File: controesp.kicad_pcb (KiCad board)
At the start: 2 copper layers, 86.5 x 84 mm, 53 parts, among them J1 Screw_Terminal_01x02, J10 Screw_Terminal_01x04, J11 Screw_Terminal_01x04, J12 Screw_Terminal_01x04, J14 Conn_01x16_Socket, J15 Screw_Terminal_01x02, J2 Screw_Terminal_01x04, J3 Conn_01x14_Socket, J4 Conn_01x14_Pin, J5 Conn_01x16_Pin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

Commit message: small progress on pcb
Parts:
- moved J6 79.1 mm to (67.5, 53.4), turned to 180 degrees
- moved J5 78.4 mm to (218.2, 67.0), turned to 90 degrees
- moved J2 77.2 mm to (101.3, 53.5), turned to 180 degrees
- moved J8 74.3 mm to (118.0, 53.4), turned to 180 degrees
- moved J3 73.5 mm to (78.5, 106.0), turned to 90 degrees
- moved J14 73.2 mm to (73.9, 74.5), turned to 90 degrees
- moved K1 69.5 mm to (40.5, 173.6)
- moved K2 69.5 mm to (57.0, 173.5)
- moved K3 69.5 mm to (40.5, 153.0)
- moved K4 69.5 mm to (56.5, 153.0)
- moved K5 69.5 mm to (73.0, 173.5)
- moved K6 69.5 mm to (89.5, 173.3)
- moved K7 69.5 mm to (73.0, 153.0)
- moved K8 69.5 mm to (89.5, 153.0)
- moved J7 68.0 mm to (84.5, 53.4), turned to 180 degrees
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
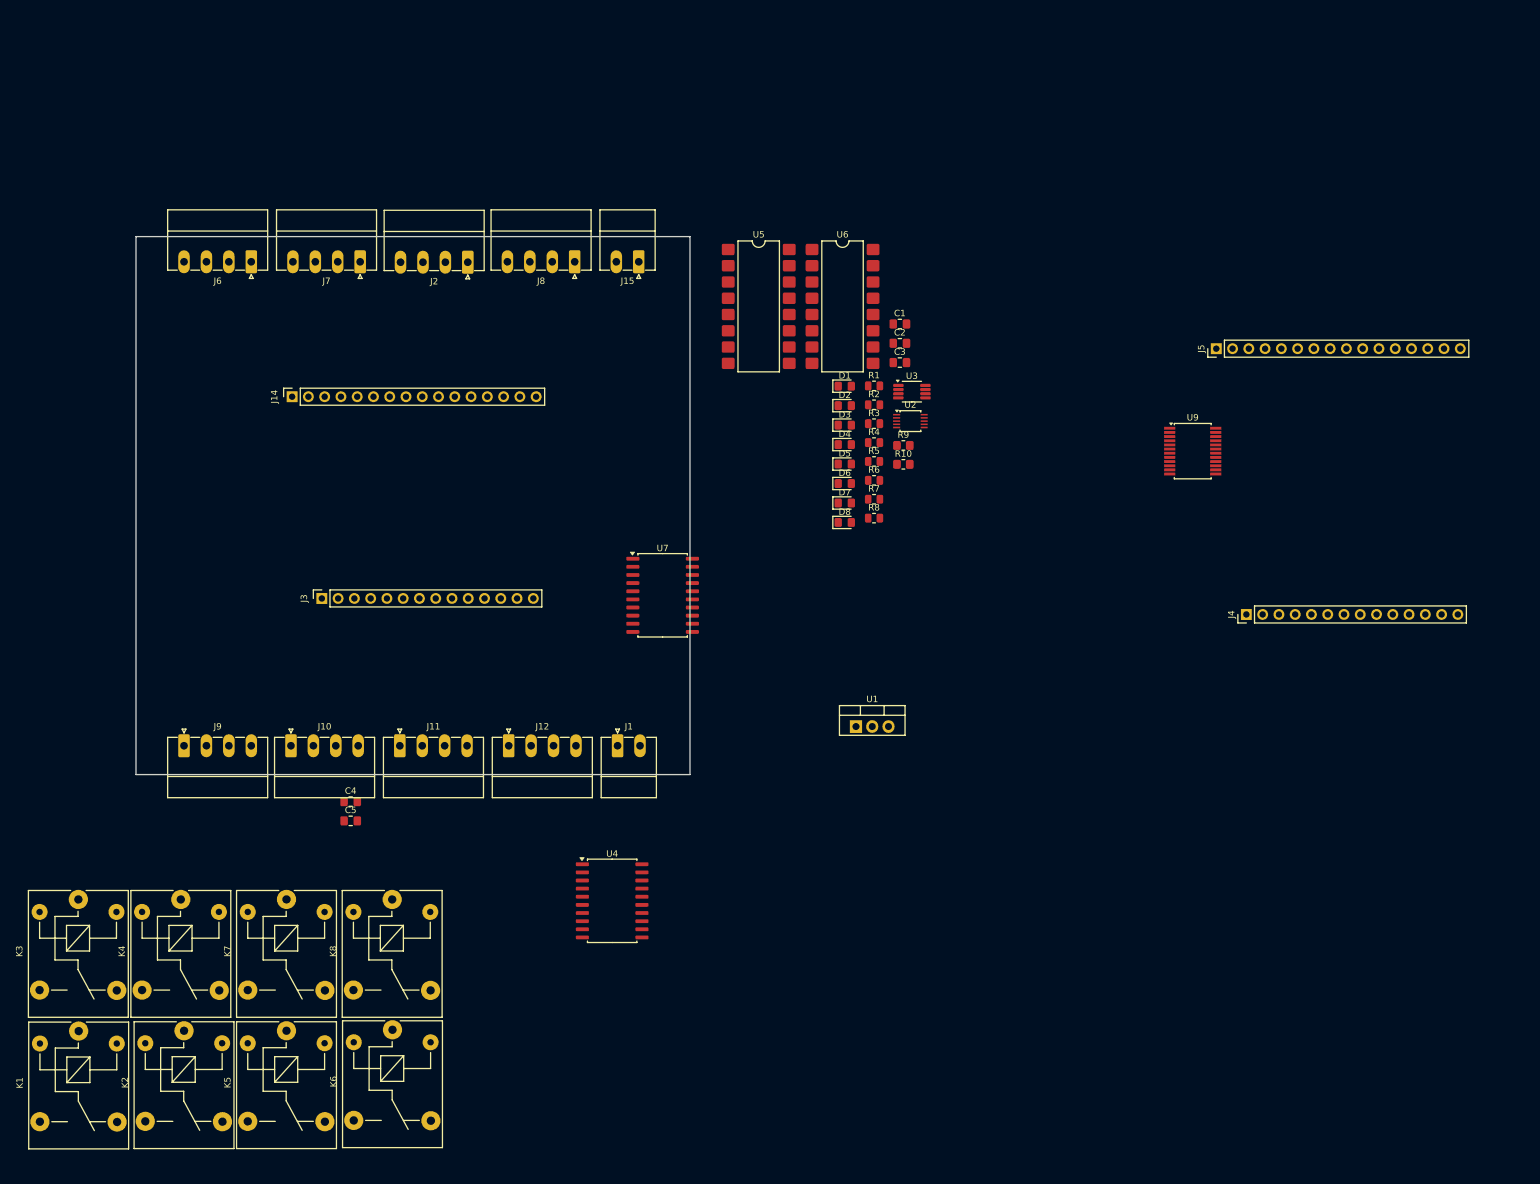
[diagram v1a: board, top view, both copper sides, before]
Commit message: larger pcb
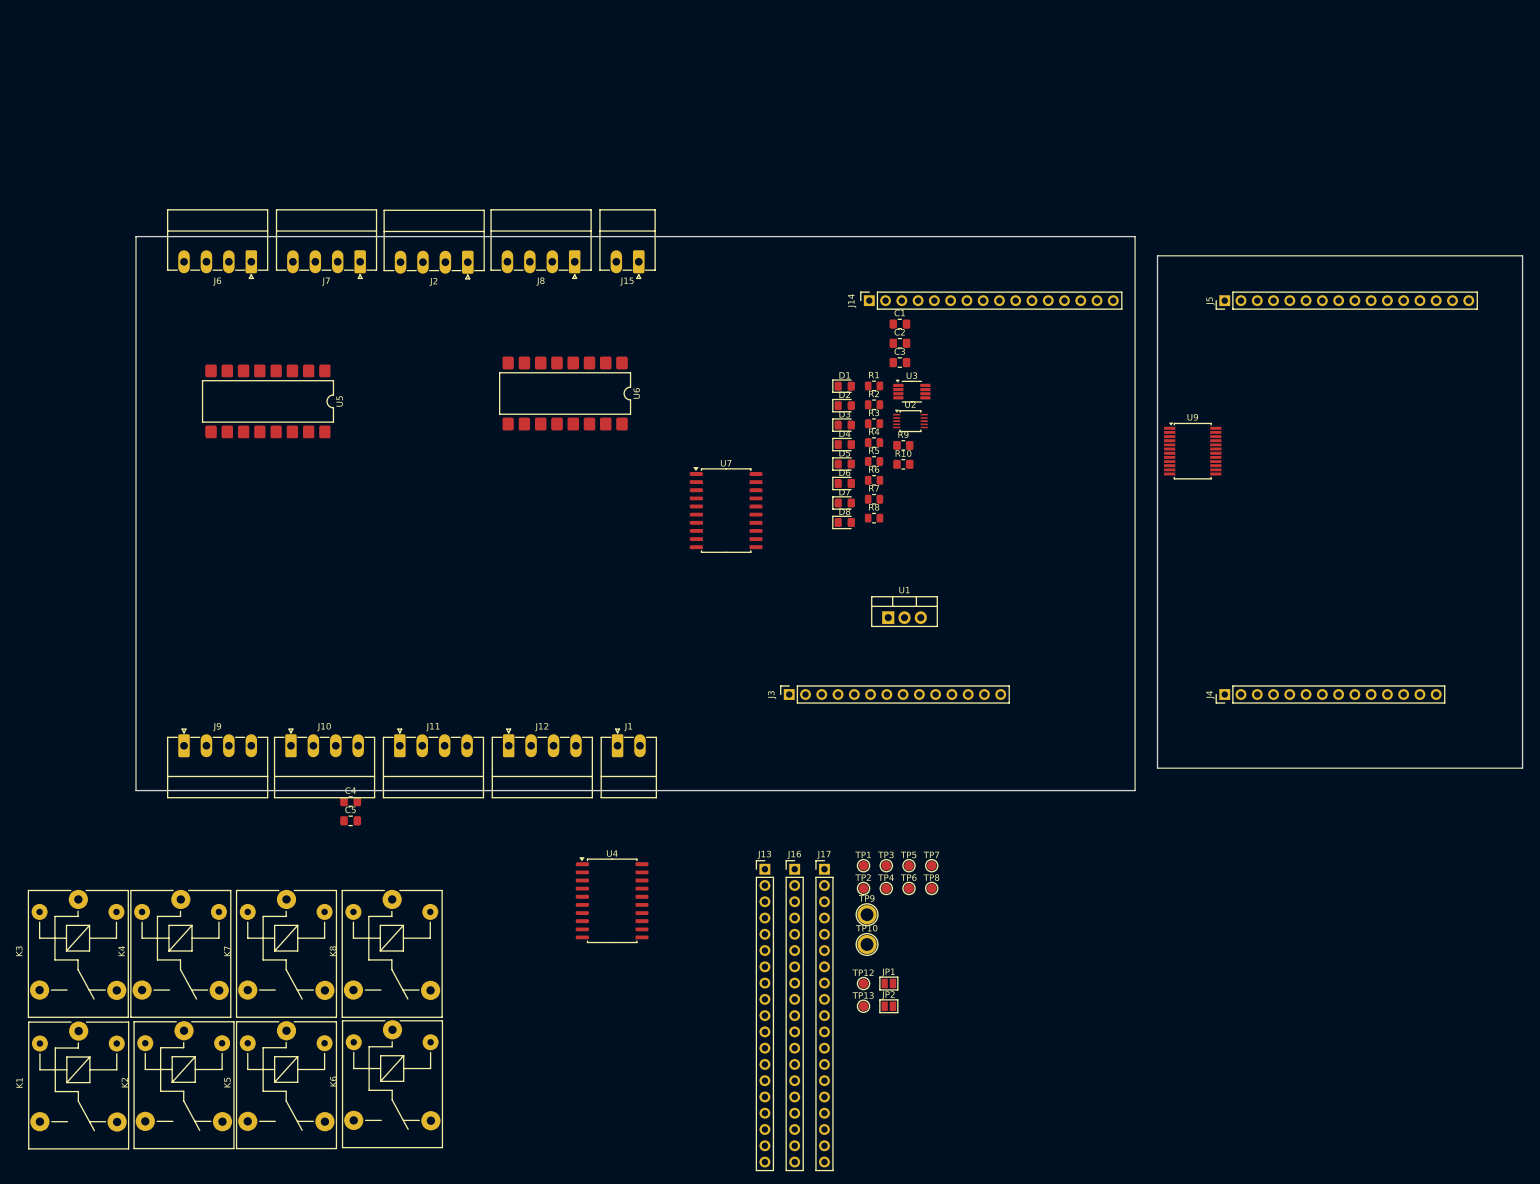
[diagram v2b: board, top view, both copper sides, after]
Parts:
- added J13: Conn_01x19_Socket, Connector_PinHeader_2.54mm:PinHeader_1x19_P2.54mm_Vertical, F.Cu at (147.7, 148.3)
- added J16: Conn_01x19_Socket, Connector_PinHeader_2.54mm:PinHeader_1x19_P2.54mm_Vertical, F.Cu at (152.3, 148.3)
- added J17: Conn_01x19_Socket, Connector_PinHeader_2.54mm:PinHeader_1x19_P2.54mm_Vertical, F.Cu at (157.0, 148.3)
- added JP1: SolderJumper_2_Open, Jumper:SolderJumper-2_P1.3mm_Open_Pad1.0x1.5mm, F.Cu at (167.1, 166.1)
- added JP2: SolderJumper_2_Open, Jumper:SolderJumper-2_P1.3mm_Open_Pad1.0x1.5mm, F.Cu at (167.1, 169.7)
- added TP1: ~, TestPoint:TestPoint_Pad_D1.5mm, F.Cu at (163.1, 147.7)
- added TP10: DO12, TestPoint:TestPoint_Plated_Hole_D2.0mm, F.Cu at (163.7, 160.0)
- added TP12: SDA, TestPoint:TestPoint_Pad_D1.5mm, F.Cu at (163.1, 166.1)
- added TP13: SCL, TestPoint:TestPoint_Pad_D1.5mm, F.Cu at (163.1, 169.7)
- added TP2: ~, TestPoint:TestPoint_Pad_D1.5mm, F.Cu at (163.1, 151.3)
- added TP3: ~, TestPoint:TestPoint_Pad_D1.5mm, F.Cu at (166.7, 147.7)
- added TP4: ~, TestPoint:TestPoint_Pad_D1.5mm, F.Cu at (166.7, 151.3)
- added TP5: ~, TestPoint:TestPoint_Pad_D1.5mm, F.Cu at (170.2, 147.7)
- added TP6: ~, TestPoint:TestPoint_Pad_D1.5mm, F.Cu at (170.2, 151.3)
- added TP7: ~, TestPoint:TestPoint_Pad_D1.5mm, F.Cu at (173.8, 147.7)
- added TP8: ~, TestPoint:TestPoint_Pad_D1.5mm, F.Cu at (173.8, 151.3)
- added TP9: DO11, TestPoint:TestPoint_Plated_Hole_D2.0mm, F.Cu at (163.7, 155.4)
- moved J14 91.4 mm to (164.0, 59.5)
- moved U5 78.0 mm to (70.1, 75.2), turned to -90 degrees
- moved J3 74.5 mm to (151.5, 121.0)
- moved U6 45.4 mm to (116.5, 74.0), turned to -90 degrees
- moved U1 17.7 mm to (167.0, 109.0)
- moved U7 16.5 mm to (141.7, 92.3)
- moved J4 12.9 mm to (219.5, 121.0)
- moved J5 7.62 mm to (219.5, 59.5)
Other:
- board size 86.5 x 84 mm -> 216.5 x 86.5 mm

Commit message: added fuse and c for 7805
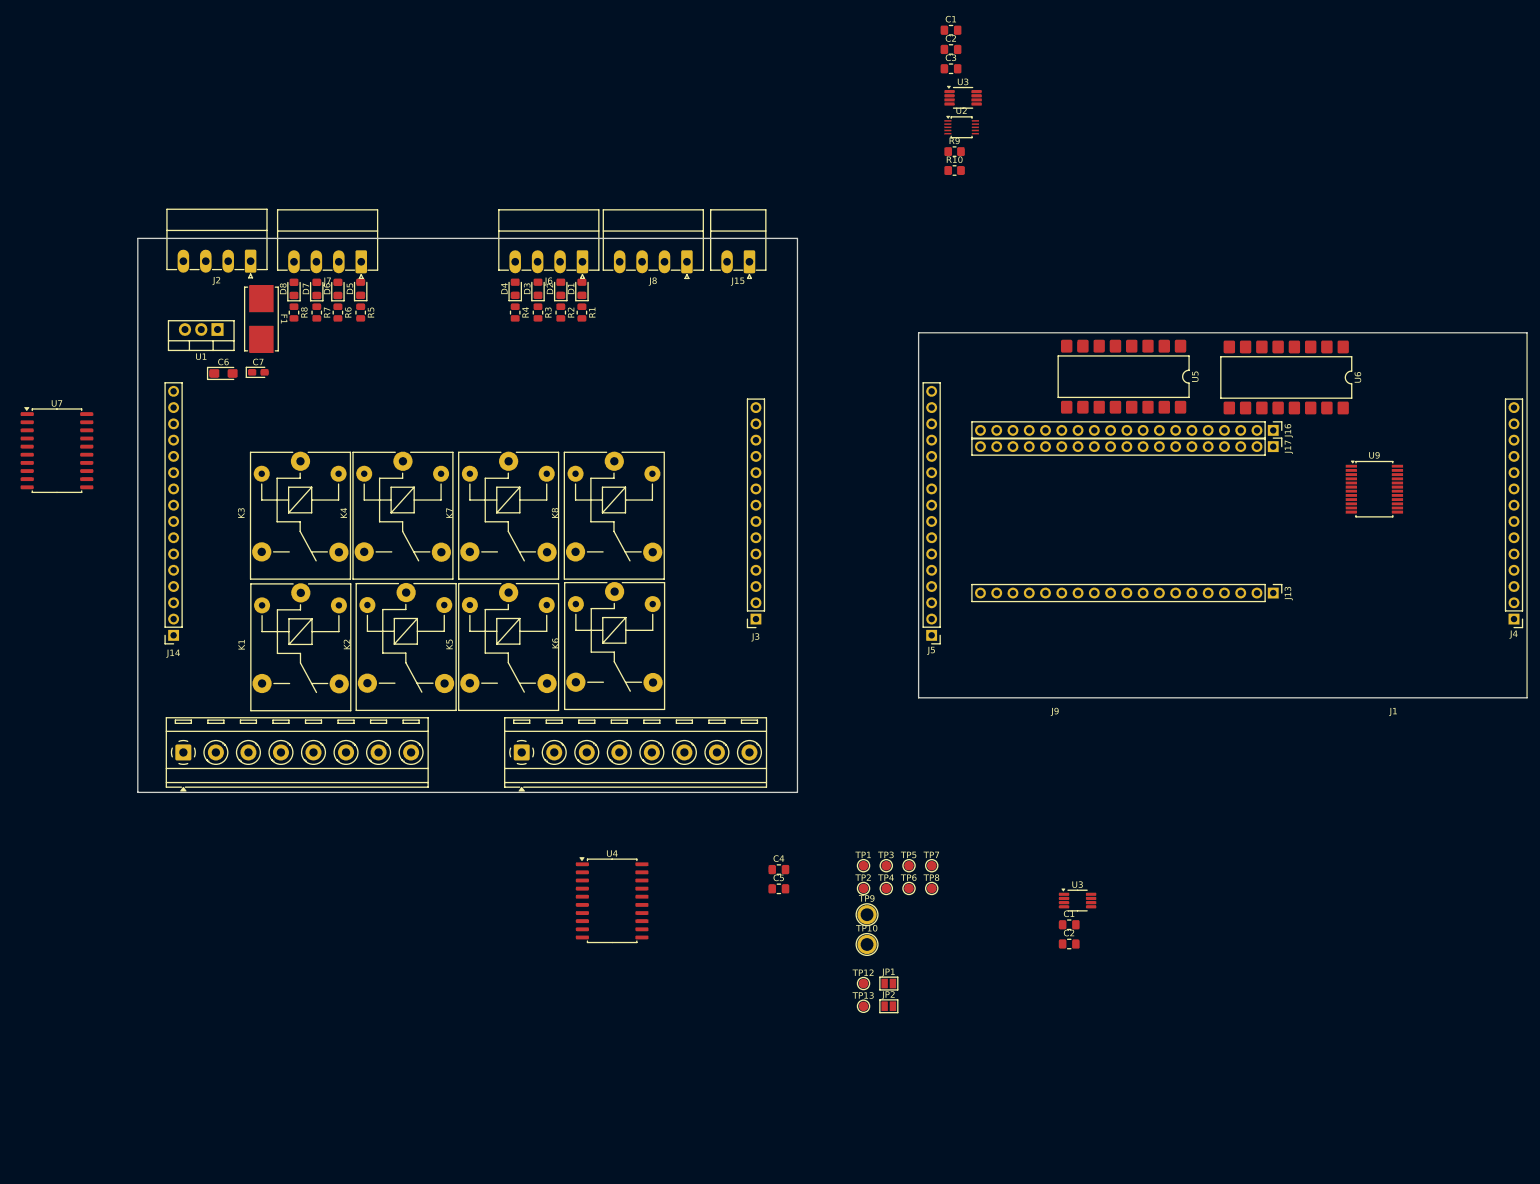
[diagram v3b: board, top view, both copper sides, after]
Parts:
- removed J10, J11, J12: Screw_Terminal_01x04, Connector_Phoenix_MC:PhoenixContact_MC_1,5_4-G-3.5_1x04_P3.50mm_Horizontal
- added C1: 100nF, Capacitor_SMD:C_0805_2012Metric_Pad1.18x1.45mm_HandSolder, F.Cu at (195.2, 157.0)
- added C2: 100nF, Capacitor_SMD:C_0805_2012Metric_Pad1.18x1.45mm_HandSolder, F.Cu at (195.2, 160.0)
- added C6: 10uF, Capacitor_Tantalum_SMD:CP_EIA-3216-12_Kemet-S_Pad1.58x1.35mm_HandSolder, F.Cu at (63.2, 70.9)
- added C7: 22uF, Capacitor_Tantalum_SMD:CP_EIA-2012-12_Kemet-R_Pad1.30x1.05mm_HandSolder, F.Cu at (68.6, 70.7)
- added F1: 1,5A, Fuse:Fuseholder_Littelfuse_Nano2_154x, F.Cu at (69.1, 62.4)
- added U3: TCA9517ADGK, Package_SO:VSSOP-8_3x3mm_P0.65mm, F.Cu at (196.5, 153.2)
- J1: value Screw_Terminal_01x02 -> Screw_Terminal_01x08; footprint Connector_Phoenix_MC:PhoenixContact_MC_1,5_2-G-3.5_1x02_P3.50mm_Horizontal -> TerminalBlock_RND:TerminalBlock_RND_205-00293_1x08_P5.08mm_Horizontal
- J9: value Screw_Terminal_01x04 -> Screw_Terminal_01x08; footprint Connector_Phoenix_MC:PhoenixContact_MC_1,5_4-G-3.5_1x04_P3.50mm_Horizontal -> TerminalBlock_RND:TerminalBlock_RND_205-00293_1x08_P5.08mm_Horizontal
- moved U5 133.7 mm to (203.7, 71.4)
- moved J14 120.5 mm to (55.4, 111.8), turned to 180 degrees
- moved U1 114.0 mm to (62.2, 64.0), turned to 180 degrees
- moved U6 112.6 mm to (229.1, 71.5)
- moved U7 104.9 mm to (37.2, 82.9)
- moved J16 101.4 mm to (227.1, 79.8), turned to -90 degrees
- moved J17 96.3 mm to (227.1, 82.3), turned to -90 degrees
- moved R8 96.1 mm to (74.2, 61.4), turned to -90 degrees
- moved D8 93.4 mm to (74.2, 57.7), turned to 90 degrees
- moved R7 91.8 mm to (77.7, 61.4), turned to -90 degrees
- moved J13 90.3 mm to (227.1, 105.2), turned to -90 degrees
- moved D7 89.0 mm to (77.7, 57.7), turned to 90 degrees
- moved R6 87.7 mm to (81.0, 61.4), turned to -90 degrees
- moved D6 84.8 mm to (81.0, 57.7), turned to 90 degrees
- moved R5 83.5 mm to (84.6, 61.4), turned to -90 degrees
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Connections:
- net /controesp_hat/GND_hat renamed /controesp_hat/GND
- net /controesp_hat/VCC_hat renamed /controesp_hat/VCC
- J1 pad 1: Net-(J1-Pin_1) -> COM1
- J13 pad 14: /controesp_hat/SDA -> SDA
- J13 pad 17: /controesp_hat/SCL -> SCL
- J2 pad 1: +24V -> Net-(J2-Pin_1)
- J3 pad 1: /powerOutput/DO1 -> DO1
- J3 pad 2: /powerOutput/DO2 -> DO2
- J3 pad 3: /powerOutput/DO3 -> DO3
- J3 pad 4: /powerOutput/DO4 -> DO4
- J3 pad 5: /powerOutput/DO5 -> DO5
- J3 pad 6: /powerOutput/DO6 -> DO6
- J5 pad 13: /controesp_hat/SCL -> /controesp_hat/SCL_5V
- J5 pad 14: /controesp_hat/SDA -> /controesp_hat/SDA_5V
- J9 pad 1: Net-(J9-Pin_1) -> COM2
- JP1 pad 2: Net-(JP1-B) -> /input/SDA
- JP2 pad 2: Net-(JP2-B) -> /input/SCL
- K1 pad 1: Net-(J9-Pin_2) -> COM1
- K1 pad 3: Net-(J9-Pin_1) -> Net-(J1-Pin_2)
- K2 pad 1: Net-(J9-Pin_4) -> COM1
- K2 pad 3: Net-(J9-Pin_3) -> Net-(J1-Pin_3)
- K3 pad 1: Net-(J10-Pin_2) -> COM1
- K3 pad 3: Net-(J10-Pin_1) -> Net-(J1-Pin_4)
- K4 pad 1: Net-(J10-Pin_4) -> COM1
- K4 pad 3: Net-(J10-Pin_3) -> Net-(J1-Pin_5)
- K5 pad 1: Net-(J11-Pin_2) -> COM2
- K5 pad 3: Net-(J11-Pin_1) -> Net-(J9-Pin_2)
- K6 pad 1: Net-(J11-Pin_4) -> COM2
- K6 pad 3: Net-(J11-Pin_3) -> Net-(J9-Pin_3)
- K7 pad 1: Net-(J12-Pin_2) -> COM2
- K7 pad 3: Net-(J12-Pin_1) -> Net-(J9-Pin_4)
- K8 pad 1: Net-(J12-Pin_4) -> COM2
- K8 pad 3: Net-(J12-Pin_3) -> Net-(J9-Pin_5)
- TP12 pad 1: Net-(JP1-B) -> /input/SDA
- TP13 pad 1: Net-(JP2-B) -> /input/SCL
- U2 pad 10: Net-(JP2-B) -> /input/SCL
- U2 pad 9: Net-(JP1-B) -> /input/SDA
- U4 pad 1: /powerOutput/DO1 -> DO1
- U4 pad 2: /powerOutput/DO2 -> DO2
- U4 pad 3: /powerOutput/DO3 -> DO3
- U4 pad 4: /powerOutput/DO4 -> DO4
- U4 pad 5: /powerOutput/DO5 -> DO5
- U4 pad 6: /powerOutput/DO6 -> DO6
- U7 pad 13: unconnected-(U7-O6-Pad13) -> DO6
- U7 pad 14: unconnected-(U7-O5-Pad14) -> DO5
- U7 pad 15: Net-(U7-O4) -> DO4
- U7 pad 16: Net-(U7-O3) -> DO3
- U7 pad 17: Net-(J1-Pin_2) -> DO2
- U7 pad 18: Net-(J1-Pin_1) -> DO1
- U9 pad 22: /controesp_hat/SCL -> /controesp_hat/SCL_5V
- U9 pad 23: /controesp_hat/SDA -> /controesp_hat/SDA_5V
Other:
- board size 216.5 x 86.5 mm -> 216.9 x 86.5 mm
